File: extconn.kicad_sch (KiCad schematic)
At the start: 21 parts

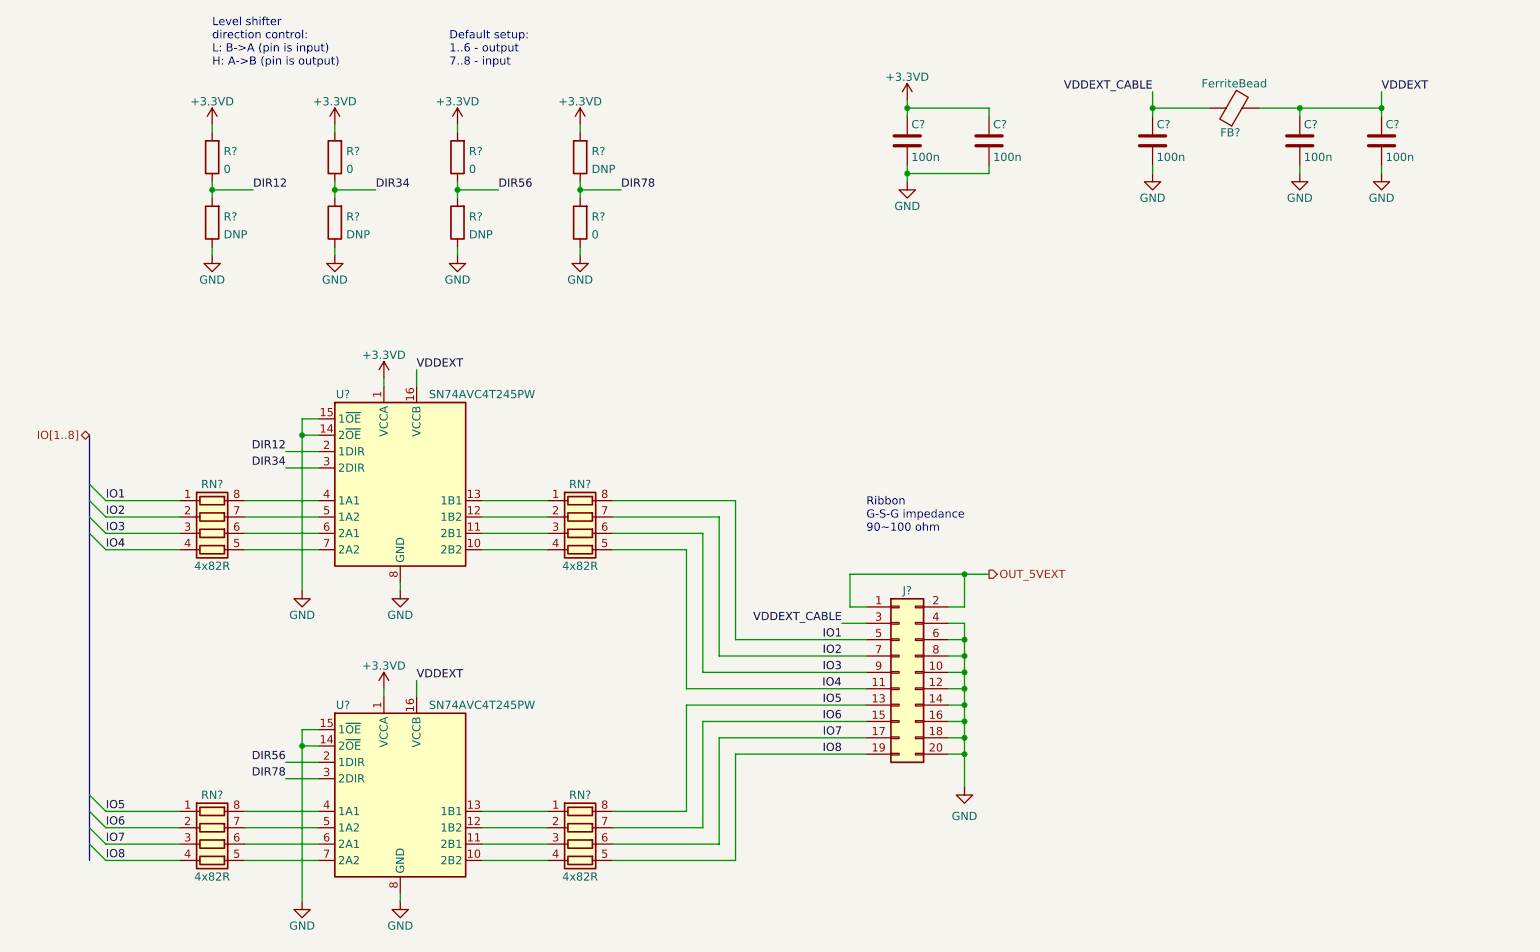
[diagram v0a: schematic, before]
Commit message: Update schematic layout, separate into sheets
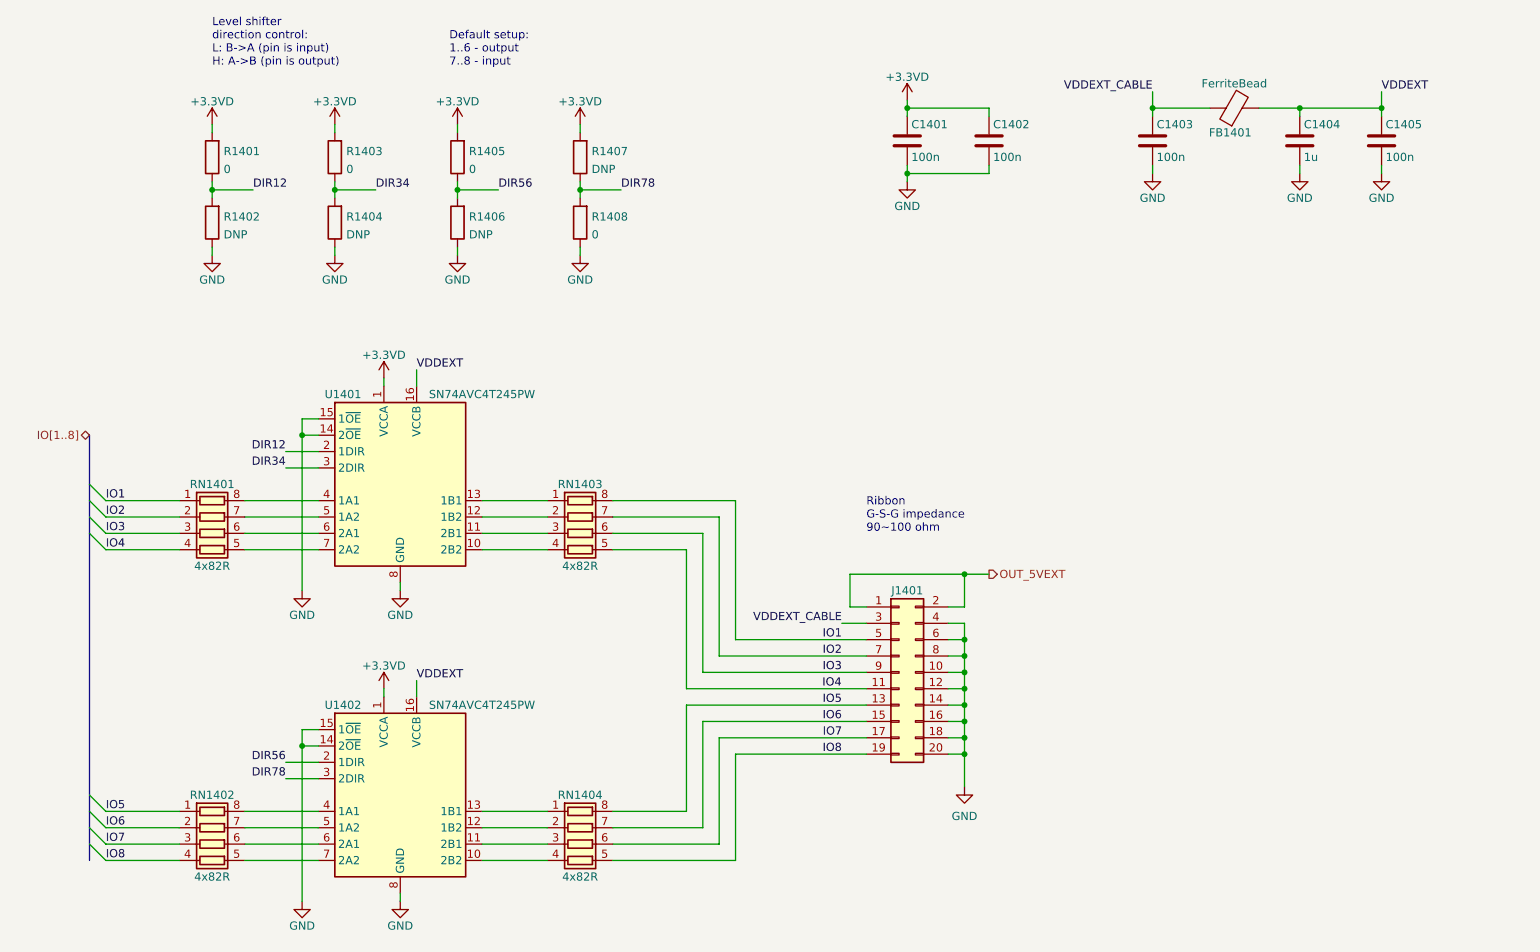
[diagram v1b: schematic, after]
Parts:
- C1404: renamed from C?; value 100n -> 1u
- gave numbers to parts that had none: 20

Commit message: Schematic update
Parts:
- added C1406: 100n, Capacitor_SMD:C_0805_2012Metric, symbol Device:C
- C1401, C1402, C1403, C1405: footprint (none) -> Capacitor_SMD:C_0805_2012Metric; Spec1 (none) -> 16V; Spec2 (none) -> X5R; Tolerance (none) -> 20%
- C1404: value 1u -> 4.7u; footprint (none) -> Capacitor_SMD:C_0805_2012Metric; Spec1 (none) -> 16V; Spec2 (none) -> X5R; Tolerance (none) -> 20%
- J1401: footprint (none) -> Connector_IDC:IDC-Header_2x10_P2.54mm_Vertical
- U1401, U1402: value SN74AVC4T245PW -> 74AVC4T245PW
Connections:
- net GND: now also C1406.2
- net VDDEXT: now also C1406.1
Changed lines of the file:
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@@
   (junction (at 186.69 138.43) (diameter 0) (color 0 0 0 0)
   )
+  (junction (at 264.16 38.1) (diameter 0) (color 0 0 0 0)
+  )
+  (junction (at 215.9 38.1) (diameter 0) (color 0 0 0 0)
+  )
+  (junction (at 186.69 125.73) (diameter 0) (color 0 0 0 0)
+  )
+  (junction (at 186.69 128.27) (diameter 0) (color 0 0 0 0)
+  )
+  (junction (at 186.69 135.89) (diameter 0) (color 0 0 0 0)
+  )
+  (junction (at 238.76 38.1) (diameter 0) (color 0 0 0 0)
+  )
+  (junction (at 177.8 38.1) (diameter 0) (color 0 0 0 0)
+  )
+  (junction (at 186.69 123.19) (diameter 0) (color 0 0 0 0)
+  )
+  (junction (at 186.69 120.65) (diameter 0) (color 0 0 0 0)
+  )
+  (junction (at 186.69 133.35) (diameter 0) (color 0 0 0 0)
+  )
   (junction (at 251.46 38.1) (diameter 0) (color 0 0 0 0)
   )
-  (junction (at 215.9 38.1) (diameter 0) (color 0 0 0 0)
-  )
-  (junction (at 186.69 125.73) (diameter 0) (color 0 0 0 0)
-  )
-  (junction (at 186.69 128.27) (diameter 0) (color 0 0 0 0)
-  )
-  (junction (at 186.69 135.89) (diameter 0) (color 0 0 0 0)
-  )
-  (junction (at 238.76 38.1) (diameter 0) (color 0 0 0 0)
-  )
-  (junction (at 177.8 38.1) (diameter 0) (color 0 0 0 0)
-  )
-  (junction (at 186.69 123.19) (diameter 0) (color 0 0 0 0)
-  )
-  (junction (at 186.69 120.65) (diameter 0) (color 0 0 0 0)
-  )
-  (junction (at 186.69 133.35) (diameter 0) (color 0 0 0 0)
-  )
   (junction (at 83.82 88.9) (diameter 0) (color 0 0 0 0)
   )
@@
     (stroke (width 0) (type default) (color 0 0 0 0))
   )
+  (wire (pts (xy 264.16 46.99) (xy 264.16 48.26))
+    (stroke (width 0) (type default) (color 0 0 0 0))
+  )
   (wire (pts (xy 99.06 160.02) (xy 99.06 161.29))
     (stroke (width 0) (type default) (color 0 0 0 0))
@@
     (stroke (width 0) (type default) (color 0 0 0 0))
   )
+  (wire (pts (xy 264.16 39.37) (xy 264.16 38.1))
+    (stroke (width 0) (type default) (color 0 0 0 0))
+  )
   (wire (pts (xy 171.45 118.11) (xy 167.64 118.11))
     (stroke (width 0) (type default) (color 0 0 0 0))
@@
     (stroke (width 0) (type default) (color 0 0 0 0))
   )
-  (wire (pts (xy 251.46 35.56) (xy 251.46 38.1))
+  (wire (pts (xy 264.16 35.56) (xy 264.16 38.1))
     (stroke (width 0) (type default) (color 0 0 0 0))
   )
@@
   )
   (wire (pts (xy 168.91 115.57) (xy 168.91 110.49))
+    (stroke (width 0) (type default) (color 0 0 0 0))
+  )
+  (wire (pts (xy 264.16 38.1) (xy 251.46 38.1))
     (stroke (width 0) (type default) (color 0 0 0 0))
   )
@@
     (effects (font (size 1.27 1.27)) (justify left bottom))
   )
-  (label "VDDEXT" (at 251.46 35.56 0)
+  (label "VDDEXT" (at 264.16 35.56 0)
     (effects (font (size 1.27 1.27)) (justify left bottom))
   )
@@
       (effects (font (size 1.27 1.27)) (justify left))
     )
-    (property "Footprint" "" (id 2) (at 191.4652 46.99 0)
+    (property "Footprint" "Capacitor_SMD:C_0805_2012Metric" (id 2) (at 191.4652 46.99 0)
       (effects (font (size 1.27 1.27)) hide)
     )
     (property "Datasheet" "~" (id 3) (at 190.5 43.18 0)
+      (effects (font (size 1.27 1.27)) hide)
+    )
+    (property "Spec1" "16V" (id 4) (at 190.5 43.18 0)
+      (effects (font (size 1.27 1.27)) hide)
+    )
+    (property "Spec2" "X5R" (id 5) (at 190.5 43.18 0)
+      (effects (font (size 1.27 1.27)) hide)
+    )
+    (property "Tolerance" "20%" (id 6) (at 190.5 43.18 0)
       (effects (font (size 1.27 1.27)) hide)
     )
@@
       (effects (font (size 1.27 1.27)) hide)
     )
-    (property "Footprint" "" (id 2) (at 176.53 125.73 0)
+    (property "Footprint" "Connector_IDC:IDC-Header_2x10_P2.54mm_Vertical" (id 2) (at 176.53 125.73 0)
       (effects (font (size 1.27 1.27)) hide)
     )
@@
       (effects (font (size 1.27 1.27)) (justify left))
     )
-    (property "Footprint" "" (id 2) (at 252.4252 46.99 0)
+    (property "Footprint" "Capacitor_SMD:C_0805_2012Metric" (id 2) (at 252.4252 46.99 0)
       (effects (font (size 1.27 1.27)) hide)
     )
     (property "Datasheet" "~" (id 3) (at 251.46 43.18 0)
+      (effects (font (size 1.27 1.27)) hide)
+    )
+    (property "Spec1" "16V" (id 4) (at 251.46 43.18 0)
+      (effects (font (size 1.27 1.27)) hide)
+    )
+    (property "Spec2" "X5R" (id 5) (at 251.46 43.18 0)
+      (effects (font (size 1.27 1.27)) hide)
+    )
+    (property "Tolerance" "20%" (id 6) (at 251.46 43.18 0)
       (effects (font (size 1.27 1.27)) hide)
     )
@@
     (in_bom yes) (on_board yes)
     (property "Reference" "U1402" (id 0) (at 90.17 130.81 0))
-    (property "Value" "SN74AVC4T245PW" (id 1) (at 111.76 130.81 0))
+    (property "Value" "74AVC4T245PW" (id 1) (at 111.76 130.81 0))
     (property "Footprint" "Package_SO:TSSOP-16_4.4x5mm_P0.65mm" (id 2) (at 99.06 147.32 0)
       (effects (font (size 1.27 1.27)) hide)
@@
     (pin "2")
   )
+  (symbol (lib_id "Device:C") (at 264.16 43.18 0) (unit 1)
+    (in_bom yes) (on_board yes)
+    (property "Reference" "C1406" (id 0) (at 264.795 40.64 0)
+      (effects (font (size 1.27 1.27)) (justify left))
+    )
+    (property "Value" "100n" (id 1) (at 264.795 45.72 0)
+      (effects (font (size 1.27 1.27)) (justify left))
+    )
+    (property "Footprint" "Capacitor_SMD:C_0805_2012Metric" (id 2) (at 265.1252 46.99 0)
+      (effects (font (size 1.27 1.27)) hide)
+    )
+    (property "Datasheet" "~" (id 3) (at 264.16 43.18 0)
+      (effects (font (size 1.27 1.27)) hide)
+    )
+    (property "Spec1" "16V" (id 4) (at 264.16 43.18 0)
+      (effects (font (size 1.27 1.27)) hide)
+    )
+    (property "Spec2" "X5R" (id 5) (at 264.16 43.18 0)
+      (effects (font (size 1.27 1.27)) hide)
+    )
+    (property "Tolerance" "20%" (id 6) (at 264.16 43.18 0)
+      (effects (font (size 1.27 1.27)) hide)
+    )
+    (pin "1")
+    (pin "2")
+  )
   (symbol (lib_id "Device:R") (at 107.95 45.72 180) (unit 1)
     (in_bom yes) (on_board yes) (fields_autoplaced)
@@
       (effects (font (size 1.27 1.27)) (justify left))
     )
-    (property "Footprint" "" (id 2) (at 178.7652 46.99 0)
+    (property "Footprint" "Capacitor_SMD:C_0805_2012Metric" (id 2) (at 178.7652 46.99 0)
       (effects (font (size 1.27 1.27)) hide)
     )
     (property "Datasheet" "~" (id 3) (at 177.8 43.18 0)
+      (effects (font (size 1.27 1.27)) hide)
+    )
+    (property "Spec1" "16V" (id 4) (at 177.8 43.18 0)
+      (effects (font (size 1.27 1.27)) hide)
+    )
+    (property "Spec2" "X5R" (id 5) (at 177.8 43.18 0)
+      (effects (font (size 1.27 1.27)) hide)
+    )
+    (property "Tolerance" "20%" (id 6) (at 177.8 43.18 0)
       (effects (font (size 1.27 1.27)) hide)
     )
@@
     (in_bom yes) (on_board yes)
     (property "Reference" "U1401" (id 0) (at 90.17 82.55 0))
-    (property "Value" "SN74AVC4T245PW" (id 1) (at 111.76 82.55 0))
+    (property "Value" "74AVC4T245PW" (id 1) (at 111.76 82.55 0))
     (property "Footprint" "Package_SO:TSSOP-16_4.4x5mm_P0.65mm" (id 2) (at 99.06 99.06 0)
       (effects (font (size 1.27 1.27)) hide)
@@
     (pin "9")
   )
+  (symbol (lib_id "power:GND") (at 264.16 48.26 0) (unit 1)
+    (in_bom yes) (on_board yes)
+    (property "Reference" "#PWR01421" (id 0) (at 264.16 54.61 0)
+      (effects (font (size 1.27 1.27)) hide)
+    )
+    (property "Value" "GND" (id 1) (at 264.16 52.07 0))
+    (property "Footprint" "" (id 2) (at 264.16 48.26 0)
+      (effects (font (size 1.27 1.27)) hide)
+    )
+    (property "Datasheet" "" (id 3) (at 264.16 48.26 0)
+      (effects (font (size 1.27 1.27)) hide)
+    )
+    (pin "1")
+  )
   (symbol (lib_id "power:GND") (at 83.82 113.03 0) (unit 1)
     (in_bom yes) (on_board yes)
@@
       (effects (font (size 1.27 1.27)) (justify left))
     )
-    (property "Footprint" "" (id 2) (at 216.8652 46.99 0)
+    (property "Footprint" "Capacitor_SMD:C_0805_2012Metric" (id 2) (at 216.8652 46.99 0)
       (effects (font (size 1.27 1.27)) hide)
     )
     (property "Datasheet" "~" (id 3) (at 215.9 43.18 0)
+      (effects (font (size 1.27 1.27)) hide)
+    )
+    (property "Spec1" "16V" (id 4) (at 215.9 43.18 0)
+      (effects (font (size 1.27 1.27)) hide)
+    )
+    (property "Spec2" "X5R" (id 5) (at 215.9 43.18 0)
+      (effects (font (size 1.27 1.27)) hide)
+    )
+    (property "Tolerance" "20%" (id 6) (at 215.9 43.18 0)
       (effects (font (size 1.27 1.27)) hide)
     )
@@
       (effects (font (size 1.27 1.27)) (justify left))
     )
-    (property "Value" "1u" (id 1) (at 239.395 45.72 0)
+    (property "Value" "4.7u" (id 1) (at 239.395 45.72 0)
       (effects (font (size 1.27 1.27)) (justify left))
     )
-    (property "Footprint" "" (id 2) (at 239.7252 46.99 0)
+    (property "Footprint" "Capacitor_SMD:C_0805_2012Metric" (id 2) (at 239.7252 46.99 0)
       (effects (font (size 1.27 1.27)) hide)
     )
@@
       (effects (font (size 1.27 1.27)) hide)
     )
+    (property "Spec1" "16V" (id 4) (at 238.76 43.18 0)
+      (effects (font (size 1.27 1.27)) hide)
+    )
+    (property "Spec2" "X5R" (id 5) (at 238.76 43.18 0)
+      (effects (font (size 1.27 1.27)) hide)
+    )
+    (property "Tolerance" "20%" (id 6) (at 238.76 43.18 0)
+      (effects (font (size 1.27 1.27)) hide)
+    )

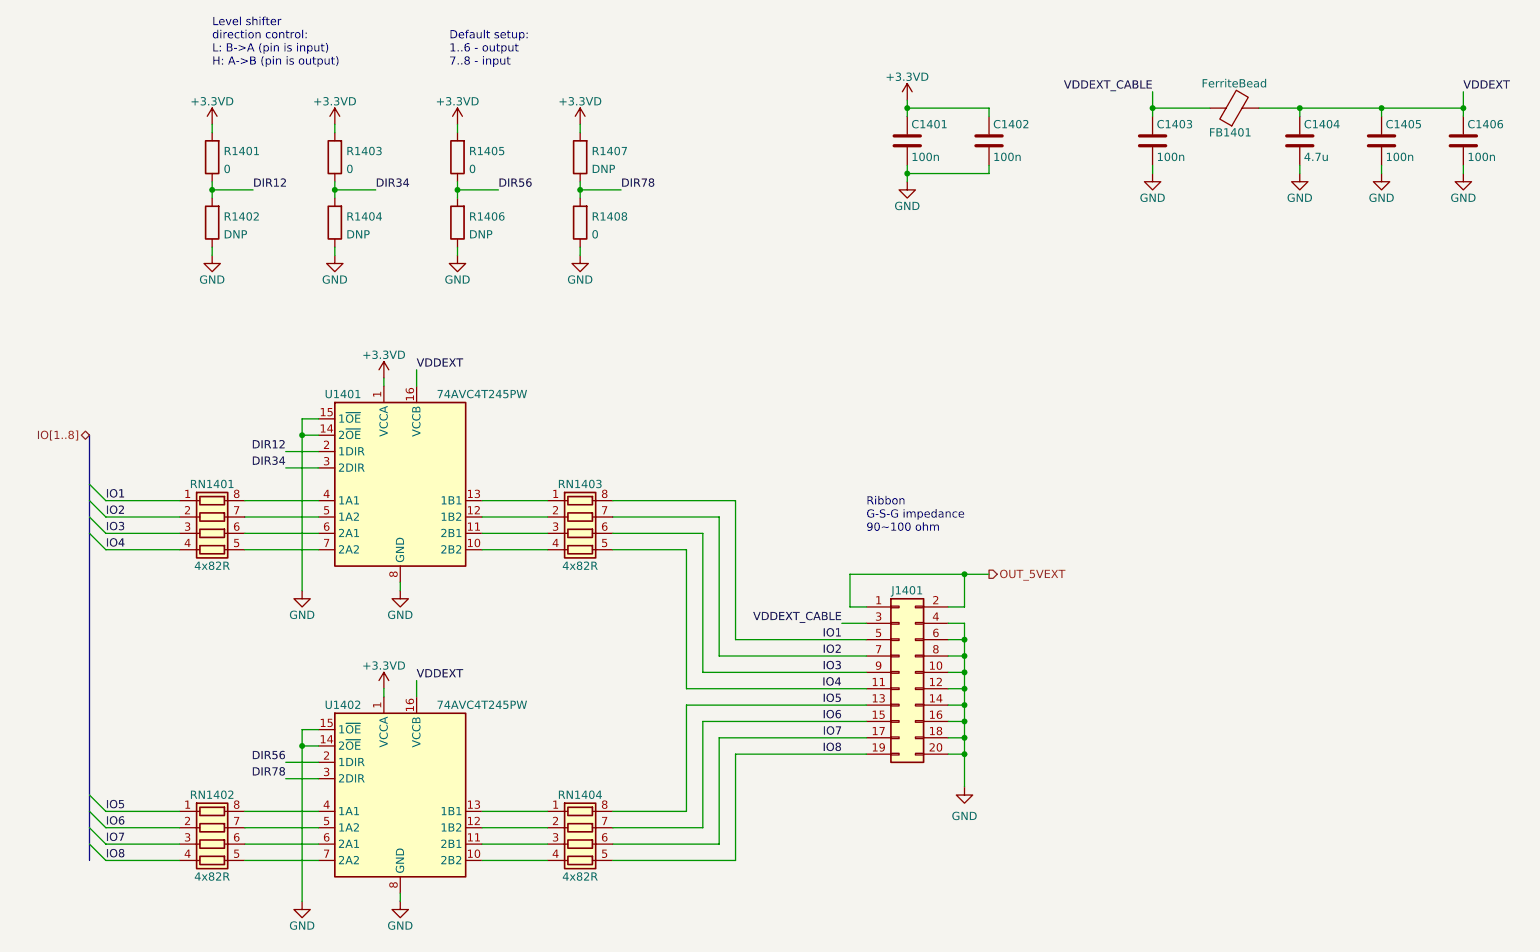
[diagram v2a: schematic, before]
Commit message: Schematic: better LDO output capacitor selection, clarified BOM
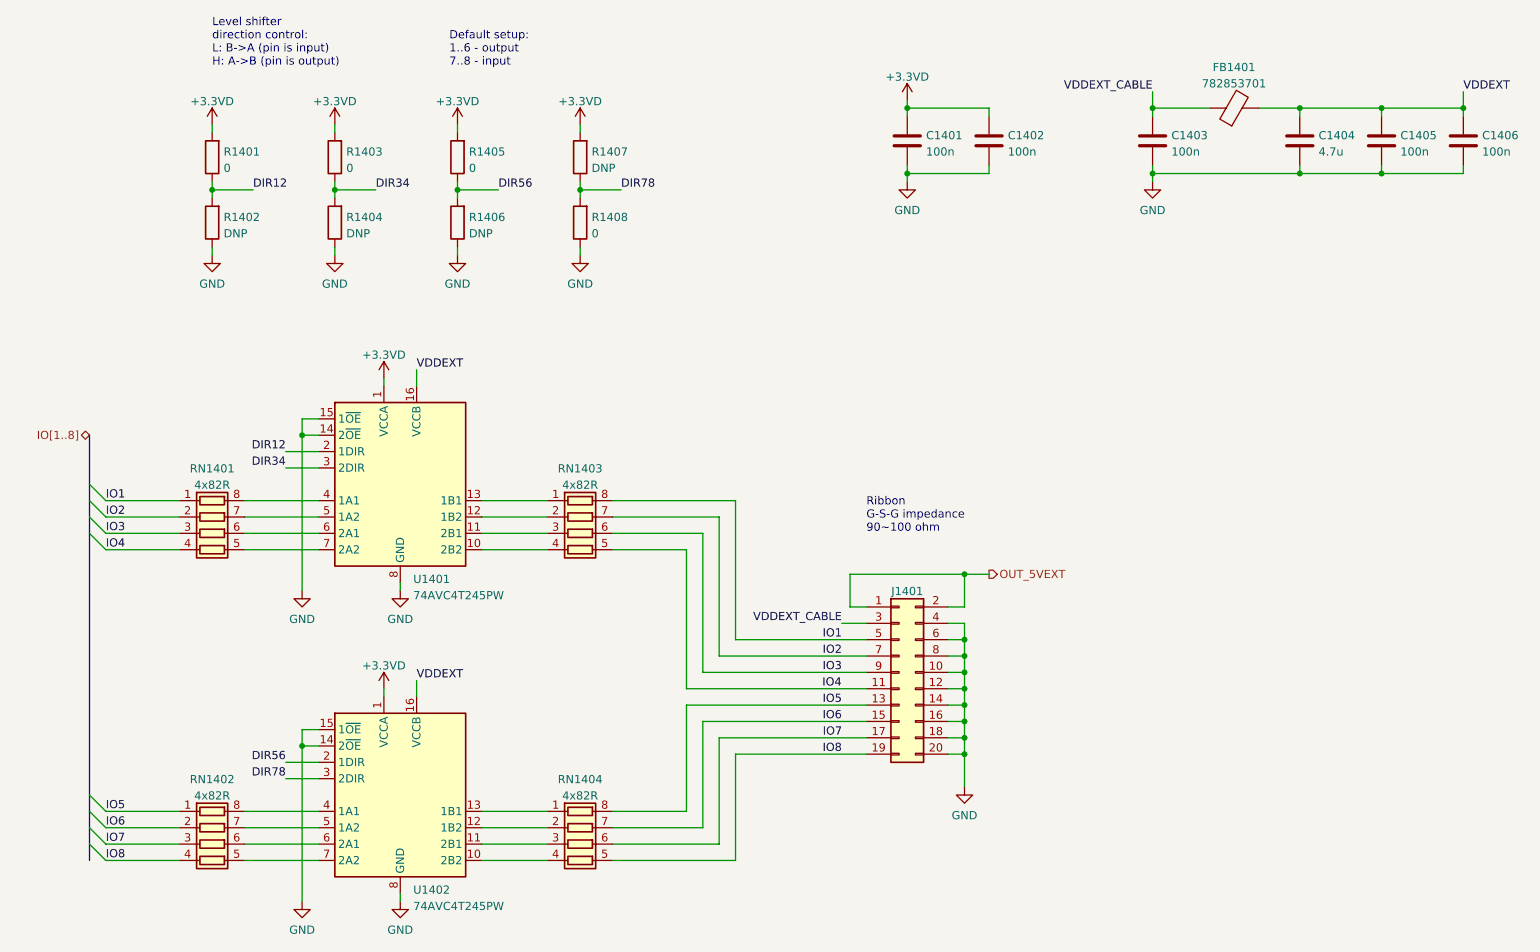
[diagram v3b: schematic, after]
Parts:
- C1401, C1402, C1403, C1404, C1405, C1406: Spec1 16V -> (none); Spec2 X5R -> (none); Tolerance 20% -> (none)
- FB1401: value FerriteBead -> 782853701; footprint (none) -> Inductor_SMD:L_0805_2012Metric_Pad1.05x1.20mm_HandSolder
